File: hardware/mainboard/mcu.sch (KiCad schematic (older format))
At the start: 17 parts, among them J2 Tag-Connect SWD, J3 USB_MICRO_RIGHT, SW1 RESET, U7 ATSAMD21G18A-AUT, U8 MCP4728

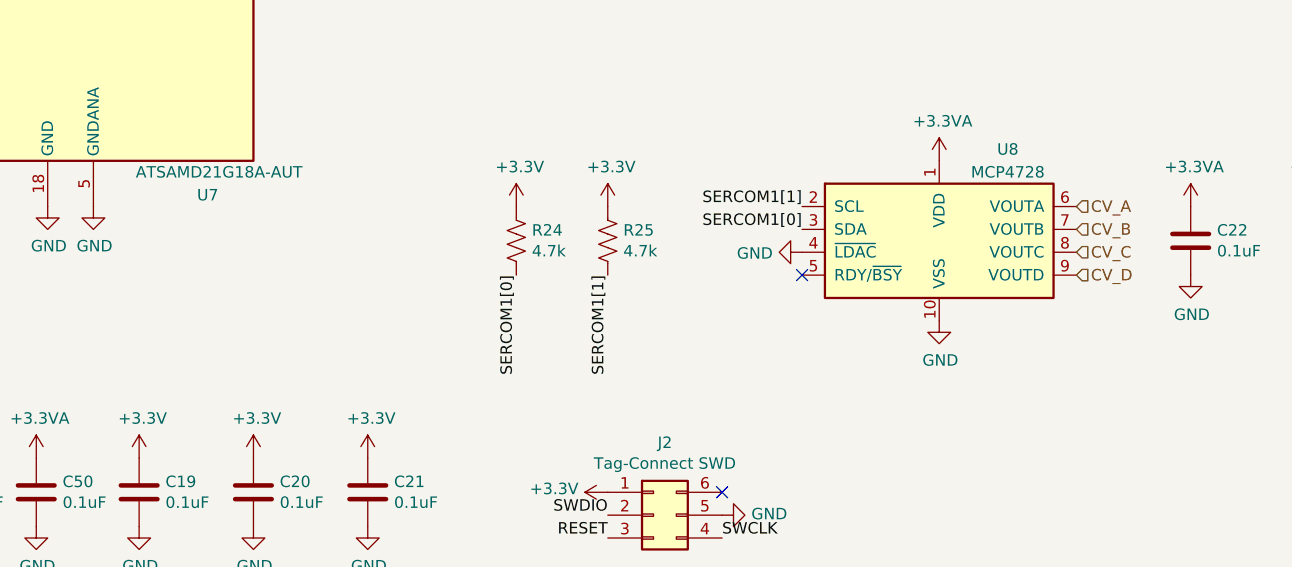
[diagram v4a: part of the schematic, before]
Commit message: Check passive ratings
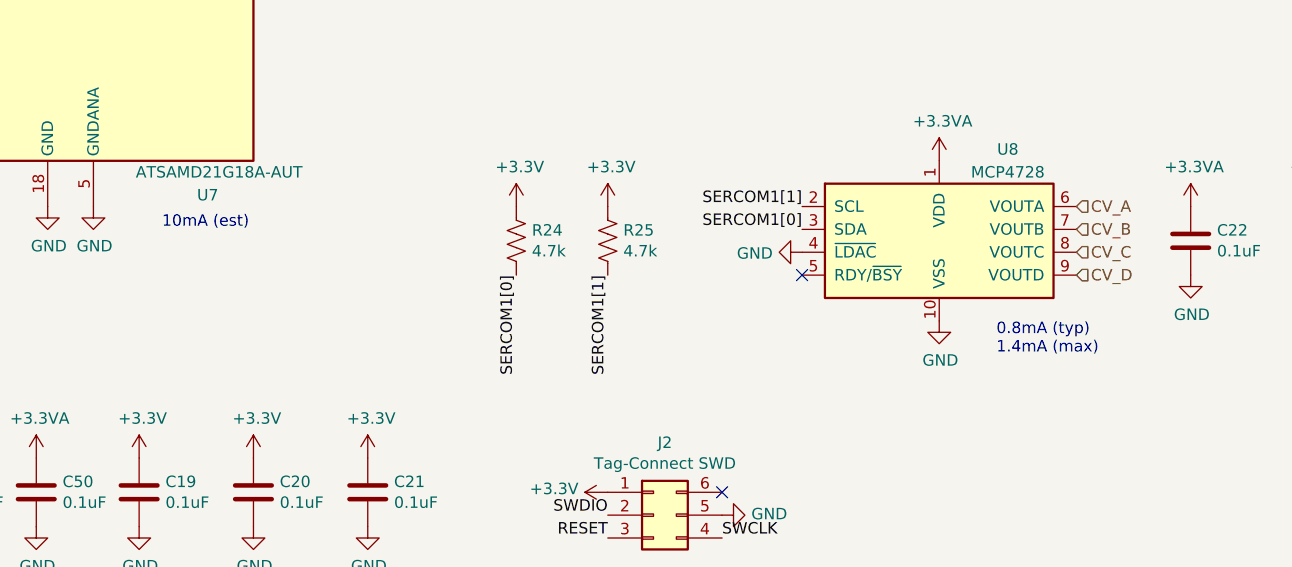
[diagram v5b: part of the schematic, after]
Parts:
- C18, C19, C20, C21, C22, C49, C50: mpn specs (none) -> 10%, 25v
- C23: mpn specs (none) -> 10% 16v
- R24, R25: mpn specs (none) -> 100mW
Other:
- note added: "0.8mA (typ)\n1.4mA (max)"
- note added: "10mA (est)"
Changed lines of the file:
@@
 F 1 "ATSAMD21G18A-AUT" H 3500 2100 50  0000 C CNN
 F 2 "Package_QFP:TQFP-48_7x7mm_P0.5mm" H 1900 2100 50  0001 C CNN
-F 3 "http://ww1.microchip.com/downloads/en/DeviceDoc/SAMD21-Family-DataSheet-DS40001882D.pdf" H 2850 4850 50  0001 C CNN
+F 3 "http://ww1.microchip.com/downloads/en/DeviceDoc/SAM_D21_DA1_Family_Data%20Sheet_DS40001882E.pdf" H 2850 4850 50  0001 C CNN
 F 4 "yes" H 2850 3850 50  0001 C CNN "finalized"
 F 5 "ATSAMD21G18A-AUT" H 2850 3850 50  0001 C CNN "mpn"
@@
 F 4 "yes" H 3050 1650 50  0001 C CNN "finalized"
 F 5 "MF-CAP-0603-1uF" H 3050 1650 50  0001 C CNN "mpn"
+F 6 "10%, 25v" H 3050 1650 50  0001 C CNN "mpn specs"
 	1    3050 1650
 	1    0    0    -1
@@
 F 4 "yes" H 3150 7000 50  0001 C CNN "finalized"
 F 5 "MF-CAP-0603-0.1uF" H 3150 7000 50  0001 C CNN "mpn"
+F 6 "10%, 25v" H 3150 7000 50  0001 C CNN "mpn specs"
 	1    3150 7000
 	1    0    0    -1
@@
 F 4 "yes" H 3650 7000 50  0001 C CNN "finalized"
 F 5 "MF-CAP-0603-0.1uF" H 3650 7000 50  0001 C CNN "mpn"
+F 6 "10%, 25v" H 3650 7000 50  0001 C CNN "mpn specs"
 	1    3650 7000
 	1    0    0    -1
@@
 F 4 "yes" H 4150 7000 50  0001 C CNN "finalized"
 F 5 "MF-CAP-0603-0.1uF" H 4150 7000 50  0001 C CNN "mpn"
+F 6 "10%, 25v" H 4150 7000 50  0001 C CNN "mpn specs"
 	1    4150 7000
 	1    0    0    -1
@@
 F 4 "yes" H 4800 5900 50  0001 C CNN "finalized"
 F 5 "MF-RES-0603-4.7K" H 4800 5900 50  0001 C CNN "mpn"
+F 6 "100mW" H 4800 5900 50  0001 C CNN "mpn specs"
 	1    4800 5900
 	1    0    0    -1
@@
 F 4 "yes" H 5200 5900 50  0001 C CNN "finalized"
 F 5 "MF-RES-0603-4.7K" H 5200 5900 50  0001 C CNN "mpn"
+F 6 "100mW" H 5200 5900 50  0001 C CNN "mpn specs"
 	1    5200 5900
 	1    0    0    -1
@@
 F 4 "yes" H 7750 5900 50  0001 C CNN "finalized"
 F 5 "MF-CAP-0603-0.1uF" H 7750 5900 50  0001 C CNN "mpn"
+F 6 "10%, 25v" H 7750 5900 50  0001 C CNN "mpn specs"
 	1    7750 5900
 	1    0    0    -1
@@
 F 4 "yes" H 8300 5900 50  0001 C CNN "finalized"
 F 5 "MF-CAP-1206-10uF" H 8300 5900 50  0001 C CNN "mpn"
+F 6 "10% 16v" H 8300 5900 50  0001 C CNN "mpn specs"
 	1    8300 5900
 	1    0    0    -1
@@
 F 4 "yes" H 2700 7000 50  0001 C CNN "finalized"
 F 5 "MF-CAP-0603-0.1uF" H 2700 7000 50  0001 C CNN "mpn"
+F 6 "10%, 25v" H 2700 7000 50  0001 C CNN "mpn specs"
 	1    2700 7000
 	1    0    0    -1
@@
 F 4 "yes" H 2250 7000 50  0001 C CNN "finalized"
 F 5 "MF-CAP-0603-0.1uF" H 2250 7000 50  0001 C CNN "mpn"
+F 6 "10%, 25v" H 2250 7000 50  0001 C CNN "mpn specs"
 	1    2250 7000
 	1    0    0    -1
@@
 TCC1WO1
 NoConn ~ 5500 3850
+Text Notes 6900 6400 0    50   ~ 0
+0.8mA (typ)\n1.4mA (max)
+Text Notes 3250 5850 0    50   ~ 0
+10mA (est)
 $EndSCHEMATC

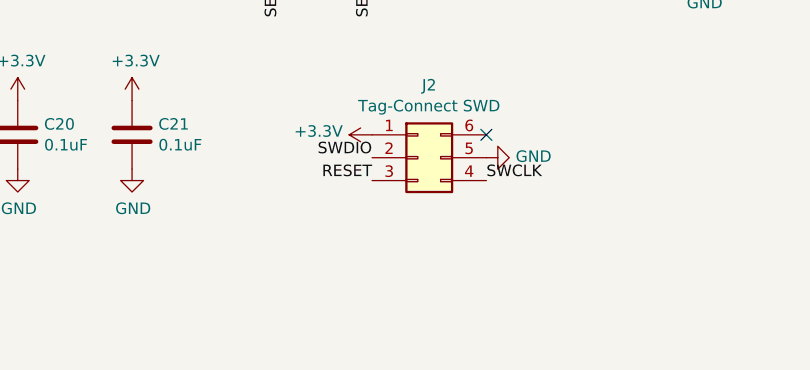
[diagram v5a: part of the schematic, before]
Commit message: Fix usb overhang, add swd pads on top copper
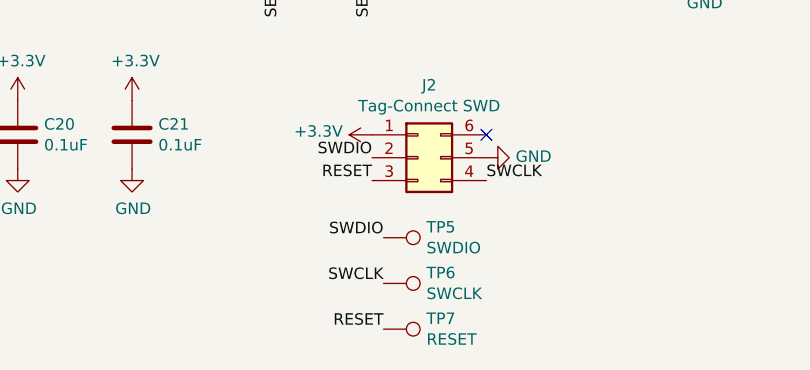
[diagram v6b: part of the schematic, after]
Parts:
- added TP5: SWDIO, TestPoint:TestPoint_Pad_D1.0mm, symbol Connector:TestPoint
- added TP6: SWCLK, TestPoint:TestPoint_Pad_D1.0mm, symbol Connector:TestPoint
- added TP7: RESET, TestPoint:TestPoint_Pad_D1.0mm, symbol Connector:TestPoint
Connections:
- net RESET: now also TP7.1
- net SWCLK: now also TP6.1
- net SWDIO: now also TP5.1
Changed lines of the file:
@@
 Text Notes 3250 5850 0    50   ~ 0
 10mA (est)
+$Comp
+L Connector:TestPoint TP5
+U 1 1 5F267ECE
+P 5250 7450
+F 0 "TP5" V 5204 7638 50  0000 L CNN
+F 1 "SWDIO" V 5295 7638 50  0000 L CNN
+F 2 "TestPoint:TestPoint_Pad_D1.0mm" H 5450 7450 50  0001 C CNN
+F 3 "~" H 5450 7450 50  0001 C CNN
+	1    5250 7450
+	0    1    1    0
+$EndComp
+$Comp
+L Connector:TestPoint TP6
+U 1 1 5F2687E0
+P 5250 7650
+F 0 "TP6" V 5204 7838 50  0000 L CNN
+F 1 "SWCLK" V 5295 7838 50  0000 L CNN
+F 2 "TestPoint:TestPoint_Pad_D1.0mm" H 5450 7650 50  0001 C CNN
+F 3 "~" H 5450 7650 50  0001 C CNN
+	1    5250 7650
+	0    1    1    0
+$EndComp
+Text Label 5250 7450 2    50   ~ 0
+SWDIO
+Text Label 5250 7650 2    50   ~ 0
+SWCLK
+Text Label 5250 7850 2    50   ~ 0
+RESET
+$Comp
+L Connector:TestPoint TP7
+U 1 1 5F2692FE
+P 5250 7850
+F 0 "TP7" V 5204 8038 50  0000 L CNN
+F 1 "RESET" V 5295 8038 50  0000 L CNN
+F 2 "TestPoint:TestPoint_Pad_D1.0mm" H 5450 7850 50  0001 C CNN
+F 3 "~" H 5450 7850 50  0001 C CNN
+	1    5250 7850
+	0    1    1    0
+$EndComp
 $EndSCHEMATC

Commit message: Bumb schematics after generating gerbers and assigning alt mpns
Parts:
- C18: mpn alt (none) -> GCM188R71E105KA64D
- C19, C20, C21, C22, C49, C50: mpn alt (none) -> GRM188R72A104KA35D
- C23: mpn alt (none) -> GRT31CR61H106ME01L
- J3: mpn alt (none) -> 10118193-0001LF
- R24, R25: mpn alt (none) -> ERA-3AED472V
- SW1: mpn alt (none) -> PTS810SJK250SMTRLFS
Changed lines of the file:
@@
 F 5 "MF-CAP-0603-1uF" H 3050 1650 50  0001 C CNN "mpn"
 F 6 "10%, 25v" H 3050 1650 50  0001 C CNN "mpn specs"
+F 7 "GCM188R71E105KA64D" H 3050 1650 50  0001 C CNN "mpn alt"
 	1    3050 1650
 	1    0    0    -1
@@
 F 4 "yes" H 1450 7000 50  0001 C CNN "finalized"
 F 5 "MF-SW-TACT-4.2MM" H 1450 7000 50  0001 C CNN "mpn"
+F 6 "PTS810SJK250SMTRLFS" H 1450 7000 50  0001 C CNN "mpn alt"
 	1    1450 7000
 	1    0    0    -1
@@
 F 5 "MF-CAP-0603-0.1uF" H 3150 7000 50  0001 C CNN "mpn"
 F 6 "10%, 25v" H 3150 7000 50  0001 C CNN "mpn specs"
+F 7 "GRM188R72A104KA35D" H 3150 7000 50  0001 C CNN "mpn alt"
 	1    3150 7000
 	1    0    0    -1
@@
 F 5 "MF-CAP-0603-0.1uF" H 3650 7000 50  0001 C CNN "mpn"
 F 6 "10%, 25v" H 3650 7000 50  0001 C CNN "mpn specs"
+F 7 "GRM188R72A104KA35D" H 3650 7000 50  0001 C CNN "mpn alt"
 	1    3650 7000
 	1    0    0    -1
@@
 F 5 "MF-CAP-0603-0.1uF" H 4150 7000 50  0001 C CNN "mpn"
 F 6 "10%, 25v" H 4150 7000 50  0001 C CNN "mpn specs"
+F 7 "GRM188R72A104KA35D" H 4150 7000 50  0001 C CNN "mpn alt"
 	1    4150 7000
 	1    0    0    -1
@@
 F 4 "yes" H 9800 5850 50  0001 C CNN "finalized"
 F 5 "MF-CON-MICROUSB-RIGHT" H 9800 5850 50  0001 C CNN "mpn"
+F 6 "10118193-0001LF" H 9800 5850 50  0001 C CNN "mpn alt"
 	1    9800 5850
 	1    0    0    -1
@@
 F 5 "MF-RES-0603-4.7K" H 4800 5900 50  0001 C CNN "mpn"
 F 6 "100mW" H 4800 5900 50  0001 C CNN "mpn specs"
+F 7 "ERA-3AED472V" H 4800 5900 50  0001 C CNN "mpn alt"
 	1    4800 5900
 	1    0    0    -1
@@
 F 5 "MF-RES-0603-4.7K" H 5200 5900 50  0001 C CNN "mpn"
 F 6 "100mW" H 5200 5900 50  0001 C CNN "mpn specs"
+F 7 "ERA-3AED472V" H 5200 5900 50  0001 C CNN "mpn alt"
 	1    5200 5900
 	1    0    0    -1
@@
 F 5 "MF-CAP-0603-0.1uF" H 7750 5900 50  0001 C CNN "mpn"
 F 6 "10%, 25v" H 7750 5900 50  0001 C CNN "mpn specs"
+F 7 "GRM188R72A104KA35D" H 7750 5900 50  0001 C CNN "mpn alt"
 	1    7750 5900
 	1    0    0    -1
@@
 F 5 "MF-CAP-1206-10uF" H 8300 5900 50  0001 C CNN "mpn"
 F 6 "10% 16v" H 8300 5900 50  0001 C CNN "mpn specs"
+F 7 "GRT31CR61H106ME01L" H 8300 5900 50  0001 C CNN "mpn alt"
 	1    8300 5900
 	1    0    0    -1
@@
 F 5 "MF-CAP-0603-0.1uF" H 2700 7000 50  0001 C CNN "mpn"
 F 6 "10%, 25v" H 2700 7000 50  0001 C CNN "mpn specs"
+F 7 "GRM188R72A104KA35D" H 2700 7000 50  0001 C CNN "mpn alt"
 	1    2700 7000
 	1    0    0    -1
@@
 F 5 "MF-CAP-0603-0.1uF" H 2250 7000 50  0001 C CNN "mpn"
 F 6 "10%, 25v" H 2250 7000 50  0001 C CNN "mpn specs"
+F 7 "GRM188R72A104KA35D" H 2250 7000 50  0001 C CNN "mpn alt"
 	1    2250 7000
 	1    0    0    -1

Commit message: Fix incorrect MPN for 10uF cap
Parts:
- C23: mpn MF-CAP-1206-10uF -> (none); mpn alt GRT31CR61H106ME01L -> GRM21BR61E106KA73K
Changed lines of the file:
@@
 F 3 "~" H 8300 5900 50  0001 C CNN
 F 4 "yes" H 8300 5900 50  0001 C CNN "finalized"
-F 5 "MF-CAP-1206-10uF" H 8300 5900 50  0001 C CNN "mpn"
+F 5 "" H 8300 5900 50  0001 C CNN "mpn"
 F 6 "10% 16v" H 8300 5900 50  0001 C CNN "mpn specs"
-F 7 "GRT31CR61H106ME01L" H 8300 5900 50  0001 C CNN "mpn alt"
+F 7 "GRM21BR61E106KA73K" H 8300 5900 50  0001 C CNN "mpn alt"
 	1    8300 5900
 	1    0    0    -1
